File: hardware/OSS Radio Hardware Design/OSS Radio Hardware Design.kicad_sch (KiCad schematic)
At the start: 38 parts, among them J1 SWD Debug, J2 USB_C_Receptacle_USB2.0_14P, SW1 SW_Push, SW2 SW_Push, U1 W25Q128JVS, U2 RP2350A-QFN60, U3 NCP1117-3.3_SOT223, Y1 ABM8-272-T3

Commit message: working on RF chip
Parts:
- added U4: SI4468-A2A-IM, QFN20_4X4_SIL, symbol 2025-03-28_00-57-05:SI4468-A2A-IM
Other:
- added sheet RF (RF.kicad_sch)
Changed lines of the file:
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@@
+	)
+	(symbol
+		(lib_id "2025-03-28_00-57-05:SI4468-A2A-IM")
+		(at 420.37 91.44 0)
+		(unit 1)
+		(exclude_from_sim no)
+		(in_bom yes)
+		(on_board yes)
+		(dnp no)
+		(fields_autoplaced yes)
+		(property "Reference" "U4"
+			(at 443.23 81.28 0)
+			(effects
+				(font
+					(size 1.524 1.524)
+				)
+			)
+		)
+		(property "Value" "SI4468-A2A-IM"
+			(at 443.23 83.82 0)
+			(effects
+				(font
+					(size 1.524 1.524)
+				)
+			)
+		)
+		(property "Footprint" "QFN20_4X4_SIL"
+			(at 420.37 91.44 0)
+			(effects
+				(font
+					(size 1.27 1.27)
+					(italic yes)
+				)
+				(hide yes)
+			)
+		)
+		(property "Datasheet" "SI4468-A2A-IM"
+			(at 420.37 91.44 0)
+			(effects
+				(font
+					(size 1.27 1.27)
+					(italic yes)
+				)
+				(hide yes)
+			)
+		)
+		(property "Description" ""
+			(at 420.37 91.44 0)
+			(effects
+				(font
+					(size 1.27 1.27)
+				)
+				(hide yes)
+			)
+		)
+		(pin "8"
+		)
+		(pin "14"
+		)
+		(pin "6"
+		)
+		(pin "3"
+		)
+		(pin "7"
+		)
+		(pin "10"
+		)
+		(pin "4"
+		)
+		(pin "1"
+		)
+		(pin "2"
+		)
+		(pin "9"
+		)
+		(pin "21"
+		)
+		(pin "20"
+		)
+		(pin "19"
+		)
+		(pin "18"
+		)
+		(pin "5"
+		)
+		(pin "17"
+		)
+		(pin "16"
+		)
+		(pin "15"
+		)
+		(pin "13"
+		)
+		(pin "12"
+		)
+		(pin "11"
+		)
+		(instances
+			(project ""
+				(path "/fd5c68a7-f5d0-4135-a258-bde3ebf63307"
+					(reference "U4")
+					(unit 1)
+				)
+			)
+		)
 	)
 	(symbol
@@
 				)
 			)
+		)
+	)
+	(sheet
+		(at 309.88 12.7)
+		(size 274.32 187.96)
+		(exclude_from_sim no)
+		(in_bom yes)
+		(on_board yes)
+		(dnp no)
+		(fields_autoplaced yes)
+		(stroke
+			(width 0.1524)
+			(type solid)
+		)
+		(fill
+			(color 0 0 0 0.0000)
+		)
+		(property "Sheetname" "RF"
+			(at 309.88 11.9884 0)
+			(effects
+				(font
+					(size 1.27 1.27)
+				)
+				(justify left bottom)
+			)
+		)
+		(property "Sheetfile" "RF.kicad_sch"
+			(at 309.88 201.2446 0)
+			(effects
+				(font
+					(size 1.27 1.27)
+				)
+				(justify left top)
+			)
+		)
+		(instances
+			(project "OSS Radio Hardware Design"
+				(path "/fd5c68a7-f5d0-4135-a258-bde3ebf63307"
+					(page "2")
+				)
+			)

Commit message: added RF IC to schematic (except for power amp)
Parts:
- removed C1, C10, C11, C12, C13, C14, C17, C18, C7, C8, C9: 100n, symbol Device:C
- removed C15, C19: 15p, symbol Device:C
- removed C16, C2, C3, C4: 4.7u, symbol Device:C
- removed C5, C6: 10u, symbol Device:C
- removed J1: SWD Debug, symbol Connector:Conn_01x03_Pin
- removed J2: USB_C_Receptacle_USB2.0_14P, symbol Connector:USB_C_Receptacle_USB2.0_14P
- removed L1: 3.3u, symbol Device:L
- removed R1: 10k, symbol Device:R
- removed R10: 0, symbol Device:R
- removed R2, R4, R5: 27, symbol Device:R
- removed R3, R6, R7: 1k, symbol Device:R
- removed R8, R9: 5k1, symbol Device:R
- removed SW1, SW2: SW_Push, symbol Switch:SW_Push
- removed U1: W25Q128JVS, Package_SO:SOIC-8_5.3x5.3mm_P1.27mm, symbol Memory_Flash:W25Q128JVS
- removed U2: RP2350A-QFN60, symbol rp2350a-qfn60:RP2350A-QFN60
- removed U3: NCP1117-3.3_SOT223, Package_TO_SOT_SMD:SOT-223-3_TabPin2, symbol Regulator_Linear:NCP1117-3.3_SOT223
- removed U4: SI4468-A2A-IM, QFN20_4X4_SIL, symbol 2025-03-28_00-57-05:SI4468-A2A-IM
- removed Y1: ABM8-272-T3, symbol Device:Crystal_GND24
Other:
- added sheet MCU (MCU.kicad_sch)
- note removed: "1.1A MAX"

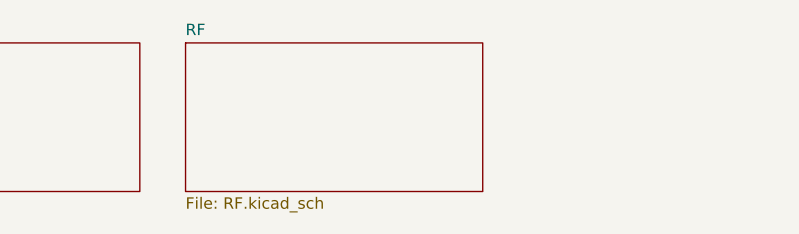
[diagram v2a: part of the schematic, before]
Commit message: working on display connector
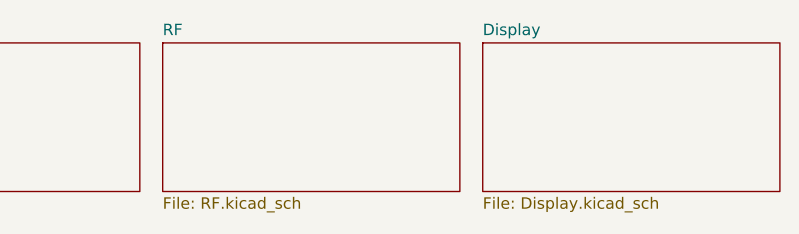
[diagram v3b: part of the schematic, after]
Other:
- added sheet Display (Display.kicad_sch)
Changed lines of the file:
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@@
 	(paper "A4")
+	(sheet
+		(at 102.87 30.48)
+		(size 33.02 16.51)
+		(exclude_from_sim no)
+		(in_bom yes)
+		(on_board yes)
+		(dnp no)
+		(fields_autoplaced yes)
+		(stroke
+			(width 0.1524)
+			(type solid)
+		)
+		(fill
+			(color 0 0 0 0.0000)
+		)
+		(property "Sheetname" "Display"
+			(at 102.87 29.7684 0)
+			(effects
+				(font
+					(size 1.27 1.27)
+				)
+				(justify left bottom)
+			)
+		)
+		(property "Sheetfile" "Display.kicad_sch"
+			(at 102.87 47.5746 0)
+			(effects
+				(font
+					(size 1.27 1.27)
+				)
+				(justify left top)
+			)
+		)
+		(instances
+			(project "OSS Radio Hardware Design"
+				(path "/fd5c68a7-f5d0-4135-a258-bde3ebf63307"
+					(page "4")
+				)
+			)
+		)
+	)
 	(sheet
 		(at 31.75 30.48)
@@
 	)
 	(sheet
-		(at 69.85 30.48)
+		(at 67.31 30.48)
 		(size 33.02 16.51)
 		(exclude_from_sim no)
@@
 		)
 		(property "Sheetname" "RF"
-			(at 69.85 29.7684 0)
+			(at 67.31 29.7684 0)
 			(effects
 				(font
@@
 		)
 		(property "Sheetfile" "RF.kicad_sch"
-			(at 69.85 47.5746 0)
+			(at 67.31 47.5746 0)
 			(effects
 				(font

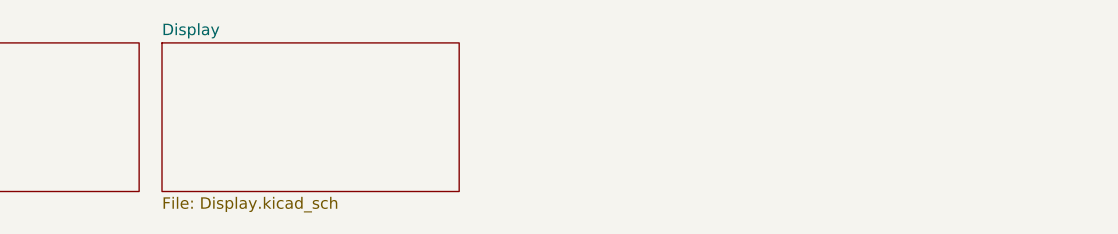
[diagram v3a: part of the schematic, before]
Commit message: schematic for sd card, external flash, working on audio amp
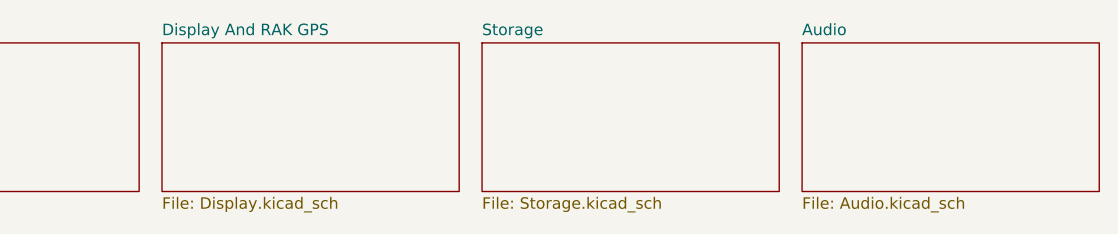
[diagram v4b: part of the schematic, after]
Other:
- sheet Display renamed Display And RAK GPS
- added sheet Audio (Audio.kicad_sch)
- added sheet Storage (Storage.kicad_sch)
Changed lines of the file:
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@@
 	(paper "A4")
 	(sheet
+		(at 173.99 30.48)
+		(size 33.02 16.51)
+		(exclude_from_sim no)
+		(in_bom yes)
+		(on_board yes)
+		(dnp no)
+		(fields_autoplaced yes)
+		(stroke
+			(width 0.1524)
+			(type solid)
+		)
+		(fill
+			(color 0 0 0 0.0000)
+		)
+		(property "Sheetname" "Audio"
+			(at 173.99 29.7684 0)
+			(effects
+				(font
+					(size 1.27 1.27)
+				)
+				(justify left bottom)
+			)
+		)
+		(property "Sheetfile" "Audio.kicad_sch"
+			(at 173.99 47.5746 0)
+			(effects
+				(font
+					(size 1.27 1.27)
+				)
+				(justify left top)
+			)
+		)
+		(instances
+			(project "OSS Radio Hardware Design"
+				(path "/fd5c68a7-f5d0-4135-a258-bde3ebf63307"
+					(page "6")
+				)
+			)
+		)
+	)
+	(sheet
 		(at 102.87 30.48)
 		(size 33.02 16.51)
@@
 			(color 0 0 0 0.0000)
 		)
-		(property "Sheetname" "Display"
+		(property "Sheetname" "Display And RAK GPS"
 			(at 102.87 29.7684 0)
 			(effects
@@
 				)
 			)
+		)
+	)
+	(sheet
+		(at 138.43 30.48)
+		(size 33.02 16.51)
+		(exclude_from_sim no)
+		(in_bom yes)
+		(on_board yes)
+		(dnp no)
+		(fields_autoplaced yes)
+		(stroke
+			(width 0.1524)
+			(type solid)
+		)
+		(fill
+			(color 0 0 0 0.0000)
+		)
+		(property "Sheetname" "Storage"
+			(at 138.43 29.7684 0)
+			(effects
+				(font
+					(size 1.27 1.27)
+				)
+				(justify left bottom)
+			)
+		)
+		(property "Sheetfile" "Storage.kicad_sch"
+			(at 138.43 47.5746 0)
+			(effects
+				(font
+					(size 1.27 1.27)
+				)
+				(justify left top)
+			)
+		)
+		(instances
+			(project "OSS Radio Hardware Design"
+				(path "/fd5c68a7-f5d0-4135-a258-bde3ebf63307"
+					(page "5")
+				)
+			)

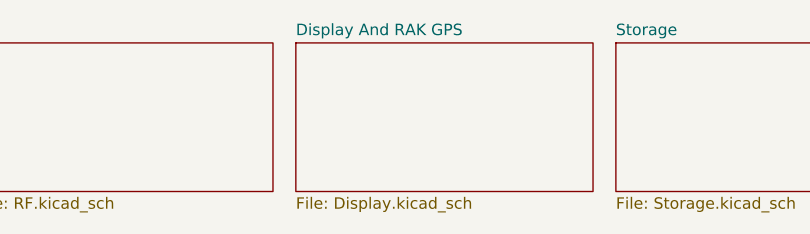
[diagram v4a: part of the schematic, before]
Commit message: finished schematic for audio
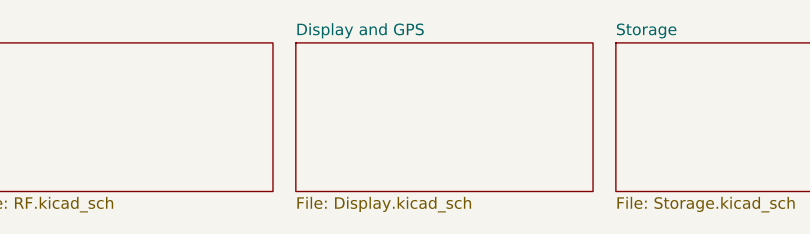
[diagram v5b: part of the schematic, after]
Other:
- sheet Display And RAK GPS renamed Display and GPS
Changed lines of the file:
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@@
 			(color 0 0 0 0.0000)
 		)
-		(property "Sheetname" "Display And RAK GPS"
+		(property "Sheetname" "Display and GPS"
 			(at 102.87 29.7684 0)
 			(effects

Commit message: working on battery circuitry
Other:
- added sheet Power (Power.kicad_sch)
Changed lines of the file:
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@@
+	)
+	(sheet
+		(at 209.55 30.48)
+		(size 33.02 16.51)
+		(exclude_from_sim no)
+		(in_bom yes)
+		(on_board yes)
+		(dnp no)
+		(fields_autoplaced yes)
+		(stroke
+			(width 0.1524)
+			(type solid)
+		)
+		(fill
+			(color 0 0 0 0.0000)
+		)
+		(property "Sheetname" "Power"
+			(at 209.55 29.7684 0)
+			(effects
+				(font
+					(size 1.27 1.27)
+				)
+				(justify left bottom)
+			)
+		)
+		(property "Sheetfile" "Power.kicad_sch"
+			(at 209.55 47.5746 0)
+			(effects
+				(font
+					(size 1.27 1.27)
+				)
+				(justify left top)
+			)
+		)
+		(instances
+			(project "OSS Radio Hardware Design"
+				(path "/fd5c68a7-f5d0-4135-a258-bde3ebf63307"
+					(page "7")
+				)
+			)
+		)
 	)
 	(sheet

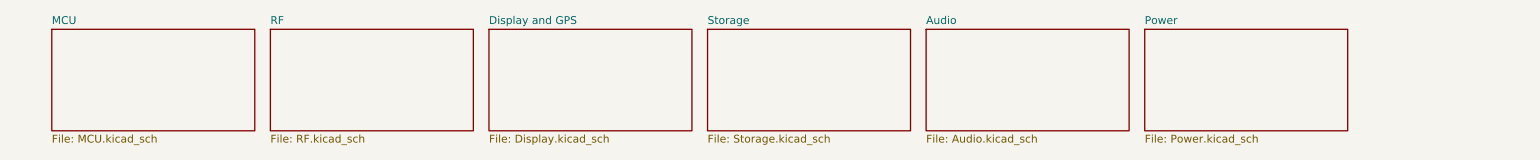
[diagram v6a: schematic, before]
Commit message: probably going to change over to PDM for audio out with an opamp
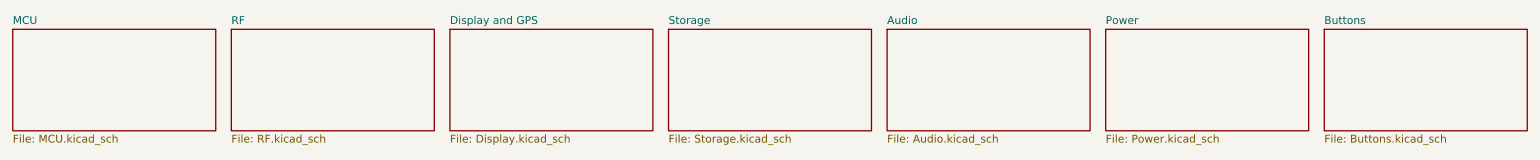
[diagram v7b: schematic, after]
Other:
- added sheet Buttons (Buttons.kicad_sch)
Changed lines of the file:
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@@
 	(paper "A4")
 	(sheet
-		(at 173.99 30.48)
+		(at 167.64 30.48)
 		(size 33.02 16.51)
 		(exclude_from_sim no)
@@
 		)
 		(property "Sheetname" "Audio"
-			(at 173.99 29.7684 0)
+			(at 167.64 29.7684 0)
 			(effects
 				(font
@@
 		)
 		(property "Sheetfile" "Audio.kicad_sch"
-			(at 173.99 47.5746 0)
+			(at 167.64 47.5746 0)
 			(effects
 				(font
@@
 	)
 	(sheet
-		(at 102.87 30.48)
+		(at 238.76 30.48)
+		(size 33.02 16.51)
+		(exclude_from_sim no)
+		(in_bom yes)
+		(on_board yes)
+		(dnp no)
+		(fields_autoplaced yes)
+		(stroke
+			(width 0.1524)
+			(type solid)
+		)
+		(fill
+			(color 0 0 0 0.0000)
+		)
+		(property "Sheetname" "Buttons"
+			(at 238.76 29.7684 0)
+			(effects
+				(font
+					(size 1.27 1.27)
+				)
+				(justify left bottom)
+			)
+		)
+		(property "Sheetfile" "Buttons.kicad_sch"
+			(at 238.76 47.5746 0)
+			(effects
+				(font
+					(size 1.27 1.27)
+				)
+				(justify left top)
+			)
+		)
+		(instances
+			(project "OSS Radio Hardware Design"
+				(path "/fd5c68a7-f5d0-4135-a258-bde3ebf63307"
+					(page "8")
+				)
+			)
+		)
+	)
+	(sheet
+		(at 96.52 30.48)
 		(size 33.02 16.51)
 		(exclude_from_sim no)
@@
 		)
 		(property "Sheetname" "Display and GPS"
-			(at 102.87 29.7684 0)
+			(at 96.52 29.7684 0)
 			(effects
 				(font
@@
 		)
 		(property "Sheetfile" "Display.kicad_sch"
-			(at 102.87 47.5746 0)
+			(at 96.52 47.5746 0)
 			(effects
 				(font
@@
 	)
 	(sheet
-		(at 209.55 30.48)
+		(at 203.2 30.48)
 		(size 33.02 16.51)
 		(exclude_from_sim no)
@@
 		)
 		(property "Sheetname" "Power"
-			(at 209.55 29.7684 0)
+			(at 203.2 29.7684 0)
 			(effects
 				(font
@@
 		)
 		(property "Sheetfile" "Power.kicad_sch"
-			(at 209.55 47.5746 0)
+			(at 203.2 47.5746 0)
 			(effects
 				(font
@@
 	)
 	(sheet
-		(at 31.75 30.48)
+		(at 25.4 30.48)
 		(size 33.02 16.51)
 		(exclude_from_sim no)
@@
 		)
 		(property "Sheetname" "MCU"
-			(at 31.75 29.7684 0)
+			(at 25.4 29.7684 0)
 			(effects
 				(font
@@
 		)
 		(property "Sheetfile" "MCU.kicad_sch"
-			(at 31.75 47.5746 0)
+			(at 25.4 47.5746 0)
 			(effects
 				(font
@@
 	)
 	(sheet
-		(at 67.31 30.48)
+		(at 60.96 30.48)
 		(size 33.02 16.51)
 		(exclude_from_sim no)
@@
 		)
 		(property "Sheetname" "RF"
-			(at 67.31 29.7684 0)
+			(at 60.96 29.7684 0)
 			(effects
 				(font
@@
 		)
 		(property "Sheetfile" "RF.kicad_sch"
-			(at 67.31 47.5746 0)
+			(at 60.96 47.5746 0)
 			(effects
 				(font
@@
 	)
 	(sheet
-		(at 138.43 30.48)
+		(at 132.08 30.48)
 		(size 33.02 16.51)
 		(exclude_from_sim no)
@@
 		)
 		(property "Sheetname" "Storage"
-			(at 138.43 29.7684 0)
+			(at 132.08 29.7684 0)
 			(effects
 				(font
@@
 		)
 		(property "Sheetfile" "Storage.kicad_sch"
-			(at 138.43 47.5746 0)
-			(effects
-				(font
+			(at 132.08 47.5746 0)
+			(effects
+				(font
